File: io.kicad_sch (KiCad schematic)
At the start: 80 parts, among them IC16 MC1489, IC19 MC1488, IC23 MC1489, IC24 82C711 SIO, X7 24MHz

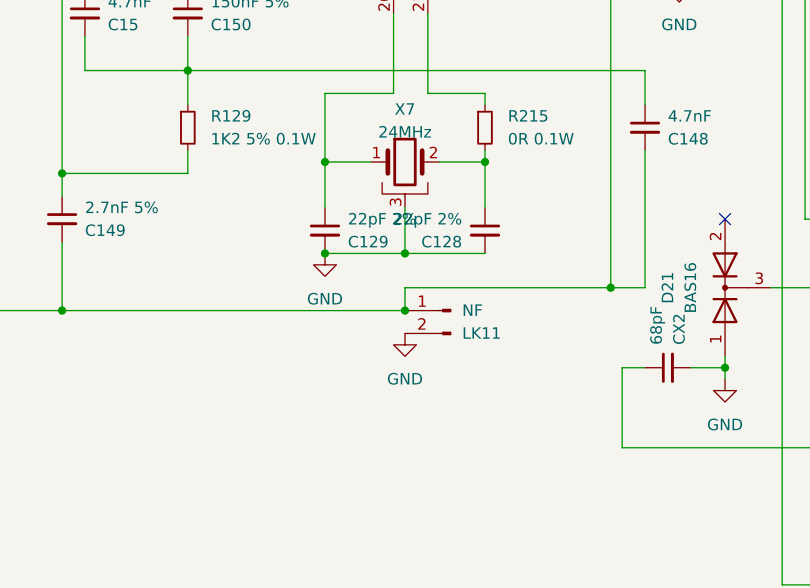
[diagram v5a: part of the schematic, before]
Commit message: switch links to net ties
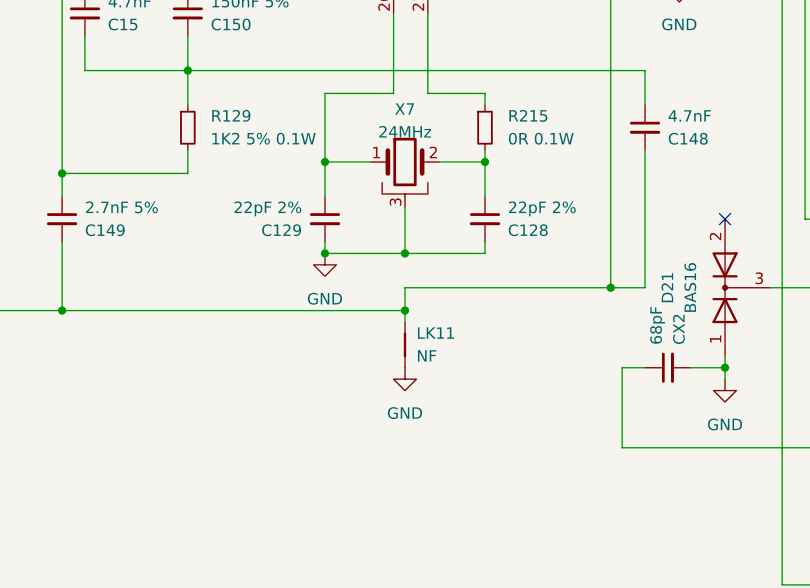
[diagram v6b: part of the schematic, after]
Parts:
- removed LK11: NF, Connector_PinHeader_2.54mm:PinHeader_1x02_P2.54mm_Vertical, symbol Connector:Conn_01x02_Pin
- added LK11: NF, Acorn:Link_Connected, symbol Device:NetTie_2
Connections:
- net GND: now also LK11.1
- net at C148.2, C149.2, IC24.98 (Avss)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: now also LK11.2
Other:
- moved on the sheet: C128, C129
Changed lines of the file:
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@@
 	)
 	(junction
-		(at 106.68 245.11)
-		(diameter 0)
-		(color 0 0 0 0)
-	)
-	(junction
 		(at 203.2 107.95)
 		(diameter 0)
@@
 	)
 	(junction
+		(at 106.68 238.76)
+		(diameter 0)
+		(color 0 0 0 0)
+	)
+	(junction
 		(at 252.73 25.4)
 		(diameter 0)
@@
 	)
 	(junction
-		(at 106.68 238.76)
-		(diameter 0)
-		(color 0 0 0 0)
-	)
-	(junction
 		(at 153.67 242.57)
 		(diameter 0)
@@
 	)
 	(junction
+		(at 106.68 245.11)
+		(diameter 0)
+		(color 0 0 0 0)
+	)
+	(junction
 		(at 217.17 143.51)
 		(diameter 0)
@@
 	(wire
 		(pts
+			(xy 97.79 237.49) (xy 97.79 238.76)
+		)
+		(stroke
+			(width 0)
+			(type default)
+		)
+	)
+	(wire
+		(pts
 			(xy 233.68 228.6) (xy 233.68 234.95)
 		)
@@
 	(wire
 		(pts
-			(xy 106.68 233.68) (xy 106.68 238.76)
-		)
-		(stroke
-			(width 0)
-			(type default)
-		)
-	)
-	(wire
-		(pts
 			(xy 215.9 57.15) (xy 242.57 57.15)
 		)
@@
 	(wire
 		(pts
-			(xy 115.57 233.68) (xy 115.57 228.6)
+			(xy 115.57 232.41) (xy 115.57 228.6)
 		)
 		(stroke
@@
 	(wire
 		(pts
+			(xy 115.57 238.76) (xy 115.57 237.49)
+		)
+		(stroke
+			(width 0)
+			(type default)
+		)
+	)
+	(wire
+		(pts
 			(xy 210.82 93.98) (xy 210.82 120.65)
 		)
@@
 	(wire
 		(pts
+			(xy 106.68 233.68) (xy 106.68 238.76)
+		)
+		(stroke
+			(width 0)
+			(type default)
+		)
+	)
+	(wire
+		(pts
 			(xy 288.29 43.18) (xy 288.29 50.8)
 		)
@@
 	(wire
 		(pts
-			(xy 97.79 228.6) (xy 97.79 233.68)
+			(xy 97.79 228.6) (xy 97.79 232.41)
 		)
 		(stroke
@@
 	(wire
 		(pts
+			(xy 106.68 245.11) (xy 106.68 246.38)
+		)
+		(stroke
+			(width 0)
+			(type default)
+		)
+	)
+	(wire
+		(pts
 			(xy 68.58 140.97) (xy 87.63 140.97)
 		)
@@
 	)
 	(symbol
-		(lib_id "Connector:Conn_01x02_Pin")
-		(at 111.76 245.11 0)
-		(mirror y)
-		(unit 1)
-		(exclude_from_sim no)
-		(in_bom yes)
-		(on_board yes)
-		(dnp no)
-		(property "Reference" "LK11"
-			(at 113.03 247.6501 0)
-			(effects
-				(font
-					(size 1.27 1.27)
-				)
-				(justify right)
-			)
-		)
-		(property "Value" "NF"
-			(at 113.03 245.1101 0)
-			(effects
-				(font
-					(size 1.27 1.27)
-				)
-				(justify right)
-			)
-		)
-		(property "Footprint" "Connector_PinHeader_2.54mm:PinHeader_1x02_P2.54mm_Vertical"
-			(at 111.76 245.11 0)
-			(effects
-				(font
-					(size 1.27 1.27)
-				)
-				(hide yes)
-			)
-		)
-		(property "Datasheet" "~"
-			(at 111.76 245.11 0)
-			(effects
-				(font
-					(size 1.27 1.27)
-				)
-				(hide yes)
-			)
-		)
-		(property "Description" "Generic connector, single row, 01x02, script generated"
-			(at 111.76 245.11 0)
-			(effects
-				(font
-					(size 1.27 1.27)
-				)
-				(hide yes)
-			)
-		)
-		(pin "1"
-		)
-		(pin "2"
-		)
-		(instances
-			(project "Acorn-A3010"
-				(path "/999882f3-94f8-4a89-9093-27a47d0cb289/b04534ef-c242-4ca8-9b8d-9d4b3e26f2f3"
-					(reference "LK11")
-					(unit 1)
-				)
-			)
-		)
-	)
-	(symbol
 		(lib_id "Connector:TestPoint")
 		(at 78.74 199.39 0)
@@
 	(symbol
 		(lib_id "power:GND")
-		(at 106.68 247.65 0)
+		(at 106.68 251.46 0)
 		(unit 1)
 		(exclude_from_sim no)
@@
 		(fields_autoplaced yes)
 		(property "Reference" "#PWR0114"
-			(at 106.68 254 0)
+			(at 106.68 257.81 0)
 			(effects
 				(font
@@
 		)
 		(property "Value" "GND"
-			(at 106.68 252.73 0)
+			(at 106.68 256.54 0)
 			(effects
 				(font
@@
 		)
 		(property "Footprint" ""
-			(at 106.68 247.65 0)
+			(at 106.68 251.46 0)
 			(effects
 				(font
@@
 		)
 		(property "Datasheet" ""
-			(at 106.68 247.65 0)
+			(at 106.68 251.46 0)
 			(effects
 				(font
@@
 		)
 		(property "Description" "Power symbol creates a global label with name \"GND\" , ground"
-			(at 106.68 247.65 0)
+			(at 106.68 251.46 0)
 			(effects
 				(font
@@
 	(symbol
 		(lib_id "Device:C_Small")
-		(at 115.57 236.22 0)
+		(at 115.57 234.95 0)
+		(mirror y)
 		(unit 1)
 		(exclude_from_sim no)
@@
 		(dnp no)
 		(property "Reference" "C128"
-			(at 113.03 237.4965 0)
+			(at 118.11 236.2265 0)
 			(effects
 				(font
@@
 		)
 		(property "Value" "22pF 2%"
-			(at 113.03 234.9565 0)
+			(at 118.11 233.6865 0)
 			(effects
 				(font
@@
 		)
 		(property "Footprint" "Capacitor_SMD:C_0805_2012Metric"
-			(at 115.57 236.22 0)
+			(at 115.57 234.95 0)
 			(effects
 				(font
@@
 		)
 		(property "Datasheet" "~"
-			(at 115.57 236.22 0)
+			(at 115.57 234.95 0)
 			(effects
 				(font
@@
 		)
 		(property "Description" "Unpolarized capacitor, small symbol"
-			(at 115.57 236.22 0)
+			(at 115.57 234.95 0)
 			(effects
 				(font
@@
 		)
 		(property "LCSC" "C1804"
-			(at 115.57 236.22 0)
+			(at 115.57 234.95 0)
 			(effects
 				(font
@@
 		)
 		(property "LCSC Part" "C1804"
-			(at 115.57 236.22 0)
+			(at 115.57 234.95 0)
 			(effects
 				(font
@@
 	)
 	(symbol
+		(lib_id "Device:NetTie_2")
+		(at 106.68 248.92 90)
+		(unit 1)
+		(exclude_from_sim no)
+		(in_bom no)
+		(on_board yes)
+		(dnp no)
+		(fields_autoplaced yes)
+		(property "Reference" "LK11"
+			(at 107.95 247.6499 90)
+			(effects
+				(font
+					(size 1.27 1.27)
+				)
+				(justify right)
+			)
+		)
+		(property "Value" "NF"
+			(at 107.95 250.1899 90)
+			(effects
+				(font
+					(size 1.27 1.27)
+				)
+				(justify right)
+			)
+		)
+		(property "Footprint" "Acorn:Link_Connected"
+			(at 106.68 248.92 0)
+			(effects
+				(font
+					(size 1.27 1.27)
+				)
+				(hide yes)
+			)
+		)
+		(property "Datasheet" "~"
+			(at 106.68 248.92 0)
+			(effects
+				(font
+					(size 1.27 1.27)
+				)
+				(hide yes)
+			)
+		)
+		(property "Description" "Net tie, 2 pins"
+			(at 106.68 248.92 0)
+			(effects
+				(font
+					(size 1.27 1.27)
+				)
+				(hide yes)
+			)
+		)
+		(pin "2"
+		)
+		(pin "1"
+		)
+		(instances
+			(project "Acorn-A3010"
+				(path "/999882f3-94f8-4a89-9093-27a47d0cb289/b04534ef-c242-4ca8-9b8d-9d4b3e26f2f3"
+					(reference "LK11")
+					(unit 1)
+				)
+			)
+		)
+	)
+	(symbol
 		(lib_id "power:GND")
 		(at 97.79 238.76 0)
@@
 	(symbol
 		(lib_id "Device:C_Small")
-		(at 97.79 236.22 0)
-		(mirror y)
+		(at 97.79 234.95 0)
 		(unit 1)
 		(exclude_from_sim no)
@@
 		(on_board yes)
 		(dnp no)
-		(fields_autoplaced yes)
 		(property "Reference" "C129"
-			(at 100.33 237.4965 0)
+			(at 95.25 236.2265 0)
 			(effects
 				(font
@@
 		)
 		(property "Value" "22pF 2%"
-			(at 100.33 234.9565 0)
+			(at 95.25 233.6865 0)
 			(effects
 				(font
@@
 		)
 		(property "Footprint" "Capacitor_SMD:C_0805_2012Metric"
-			(at 97.79 236.22 0)
+			(at 97.79 234.95 0)
 			(effects
 				(font
@@
 		)
 		(property "Datasheet" "~"
-			(at 97.79 236.22 0)
+			(at 97.79 234.95 0)
 			(effects
 				(font
@@
 		)
 		(property "Description" "Unpolarized capacitor, small symbol"
-			(at 97.79 236.22 0)
+			(at 97.79 234.95 0)
 			(effects
 				(font
@@
 		)
 		(property "LCSC" "C1804"
-			(at 97.79 236.22 0)
+			(at 97.79 234.95 0)
 			(effects
 				(font
@@
 		)
 		(property "LCSC Part" "C1804"
-			(at 97.79 236.22 0)
+			(at 97.79 234.95 0)
 			(effects
 				(font
